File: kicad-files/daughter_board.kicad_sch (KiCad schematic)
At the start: 14 parts, among them J1 TYPE-C-31-M12_13, T1 53261-0471, U2 USBLC6-2SC6, U4 SGM2007-3.3XN5/TR

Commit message: SMall changes to the db
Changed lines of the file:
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@@
   (junction (at 133.35 147.32) (diameter 0) (color 0 0 0 0)
   )
-  (junction (at 148.59 113.03) (diameter 0) (color 0 0 0 0)
+  (junction (at 161.29 113.03) (diameter 0) (color 0 0 0 0)
   )
   (junction (at 148.59 120.65) (diameter 0) (color 0 0 0 0)
@@
   )
   (wire (pts (xy 148.59 83.82) (xy 167.64 83.82))
+    (stroke (width 0) (type default))
+  )
+  (wire (pts (xy 161.29 113.03) (xy 179.07 113.03))
     (stroke (width 0) (type default))
   )
@@
     (stroke (width 0) (type default))
   )
-  (wire (pts (xy 148.59 113.03) (xy 179.07 113.03))
-    (stroke (width 0) (type default))
-  )
   (wire (pts (xy 236.22 127) (xy 191.77 127))
     (stroke (width 0) (type default))
@@
   )
   (wire (pts (xy 243.84 71.12) (xy 248.92 71.12))
+    (stroke (width 0) (type default))
+  )
+  (wire (pts (xy 148.59 110.49) (xy 161.29 110.49))
     (stroke (width 0) (type default))
   )
@@
     (stroke (width 0) (type default))
   )
+  (wire (pts (xy 148.59 113.03) (xy 161.29 113.03))
+    (stroke (width 0) (type default))
+  )
   (wire (pts (xy 232.41 106.68) (xy 232.41 134.62))
     (stroke (width 0) (type default))
@@
     (stroke (width 0) (type default))
   )
+  (wire (pts (xy 161.29 110.49) (xy 161.29 113.03))
+    (stroke (width 0) (type default))
+  )
   (wire (pts (xy 190.5 66.04) (xy 190.5 71.12))
     (stroke (width 0) (type default))
@@
     (stroke (width 0) (type default))
   )
-  (wire (pts (xy 148.59 110.49) (xy 148.59 113.03))
-    (stroke (width 0) (type default))
-  )

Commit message: Fixed up the daughter board
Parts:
- removed U2: USBLC6-2SC6, acheron_Components:SOT-23-6, symbol Power_Protection:USBLC6-2SC6
- added D1: ESD5Z5V0, Diode_SMD:D_SOD-523, symbol Diode:SMF6V0A
- added U1: TPD4E05U06DQAR, Package_SON:USON-10_2.5x1.0mm_P0.5mm, symbol acheron_Symbols:TPD4E05U06DQAR
- D1: value B5819W-SL -> 1N5819WS; footprint Diode_SMD:D_SOD-123 -> Diode_SMD:D_SOD-323
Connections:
- net GND: now also D1.1 (A1), U1.3 (GND), U1.8 (GND)
- net 3V3: now reaches C5.1, D1.2 (A), R4.2, T1.1 (3V3), U4.5 (OUT)
- net VBUS: now reaches F1.1, J1.A4 (VBUS), J1.B4 (VBUS)
- net VBUS: now also D1.2 (A2)
- net D+: now reaches T1.2 (D+)
- net D+: now also J1.A6 (D+), J1.B6 (D+), U1.4 (D2+), U1.5 (D2-), U1.6 (NC), U1.7 (NC)
- net D-: now reaches T1.3 (D-)
- net D-: now also J1.A7 (D-), J1.B7 (D-), U1.1 (IO1), U1.10 (NC), U1.2 (IO2), U1.9 (NC)
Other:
- moved on the sheet: C3, C4, C5, D1, F1, FB1, J1, R1, R2, R3, R4, U4

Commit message: Finished daughter board
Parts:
- added MH1, MH3, MH4: Mount-M2, MountingHole:MountingHole_2.2mm_M2_Pad_TopOnly, symbol Connector_Generic:Conn_01x01
- added MH2: Mount-M2, MountingHole:MountingHole_2.2mm_M2_Pad_TopBottom, symbol Connector_Generic:Conn_01x01
- C3, C4, C5: footprint Capacitor_SMD:C_0603_1608Metric_Pad1.08x0.95mm_HandSolder -> Capacitor_SMD:C_0402_1005Metric
- D1: footprint Diode_SMD:D_SOD-323 -> Diode_SMD:D_SOD-123
- R1, R2, R3, R4: footprint Resistor_SMD:R_0603_1608Metric -> Resistor_SMD:R_0402_1005Metric
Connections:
- net GNDPWR: now also MH2.1 (Pin_1)
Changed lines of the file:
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@@
       (effects (font (size 1.27 1.27)))
     )
-    (property "Footprint" "Resistor_SMD:R_0603_1608Metric" (at 242.316 85.09 90)
+    (property "Footprint" "Resistor_SMD:R_0402_1005Metric" (at 242.316 85.09 90)
       (effects (font (size 1.27 1.27)) hide)
     )
@@
       (effects (font (size 1.27 1.27)))
     )
-    (property "Footprint" "Resistor_SMD:R_0603_1608Metric" (at 205.486 85.09 90)
+    (property "Footprint" "Resistor_SMD:R_0402_1005Metric" (at 205.486 85.09 90)
       (effects (font (size 1.27 1.27)) hide)
     )
@@
     )
   )
+  (symbol (lib_id "power:GNDPWR") (at 236.855 124.587 270) (unit 1)
+    (in_bom yes) (on_board yes) (dnp no)
+    (property "Reference" "#PWR06" (at 231.775 124.587 0)
+      (effects (font (size 1.27 1.27)) hide)
+    )
+    (property "Value" "GNDPWR" (at 234.315 124.587 0)
+      (effects (font (size 0.381 0.381)) hide)
+    )
+    (property "Footprint" "" (at 235.585 124.587 0)
+      (effects (font (size 1.27 1.27)) hide)
+    )
+    (property "Datasheet" "" (at 235.585 124.587 0)
+      (effects (font (size 1.27 1.27)) hide)
+    )
+    (pin "1")
+    (instances
+      (project "daughter_board"
+        (path "/5fbc77d5-0b17-4c7b-9496-7422d8d21889"
+          (reference "#PWR06") (unit 1)
+        )
+      )
+      (project "UDB"
+        (path "/c4c12ac1-bf97-4e49-b99b-b461a52b064e"
+          (reference "#PWR03") (unit 1)
+        )
+      )
+    )
+  )
   (symbol (lib_id "power:GND") (at 220.218 90.17 0) (unit 1)
     (in_bom yes) (on_board yes) (dnp no) (fields_autoplaced)
@@
     )
   )
+  (symbol (lib_id "Connector_Generic:Conn_01x01") (at 241.935 124.587 0) (unit 1)
+    (in_bom no) (on_board yes) (dnp no)
+    (property "Reference" "MH2" (at 243.9416 123.5202 0)
+      (effects (font (size 1.27 1.27)) (justify left))
+    )
+    (property "Value" "Mount-M2" (at 243.9416 125.8316 0)
+      (effects (font (size 1.27 1.27)) (justify left))
+    )
+    (property "Footprint" "MountingHole:MountingHole_2.2mm_M2_Pad_TopBottom" (at 241.935 124.587 0)
+      (effects (font (size 1.27 1.27)) hide)
+    )
+    (property "Datasheet" "~" (at 241.935 124.587 0)
+      (effects (font (size 1.27 1.27)) hide)
+    )
+    (pin "1")
+    (instances
+      (project "daughter_board"
+        (path "/5fbc77d5-0b17-4c7b-9496-7422d8d21889"
+          (reference "MH2") (unit 1)
+        )
+      )
+      (project "UDB"
+        (path "/c4c12ac1-bf97-4e49-b99b-b461a52b064e"
+          (reference "MH2") (unit 1)
+        )
+      )
+    )
+  )
   (symbol (lib_id "Device:D_Schottky") (at 220.218 68.58 0) (unit 1)
     (in_bom yes) (on_board yes) (dnp no) (fields_autoplaced)
@@
       (effects (font (size 1.27 1.27)))
     )
-    (property "Footprint" "Diode_SMD:D_SOD-323" (at 220.218 68.58 0)
+    (property "Footprint" "Diode_SMD:D_SOD-123" (at 220.218 68.58 0)
       (effects (font (size 1.27 1.27)) hide)
     )
@@
       (effects (font (size 1.27 1.27)) (justify left))
     )
-    (property "Footprint" "Capacitor_SMD:C_0603_1608Metric_Pad1.08x0.95mm_HandSolder" (at 251.6632 88.9 0)
+    (property "Footprint" "Capacitor_SMD:C_0402_1005Metric" (at 251.6632 88.9 0)
       (effects (font (size 1.27 1.27)) hide)
     )
@@
       (effects (font (size 1.27 1.27)))
     )
-    (property "Footprint" "Resistor_SMD:R_0603_1608Metric" (at 135.382 90.678 90)
+    (property "Footprint" "Resistor_SMD:R_0402_1005Metric" (at 135.382 90.678 90)
       (effects (font (size 1.27 1.27)) hide)
     )
@@
       (effects (font (size 1.27 1.27)) (justify left))
     )
-    (property "Footprint" "Capacitor_SMD:C_0603_1608Metric_Pad1.08x0.95mm_HandSolder" (at 198.3232 88.9 0)
+    (property "Footprint" "Capacitor_SMD:C_0402_1005Metric" (at 198.3232 88.9 0)
       (effects (font (size 1.27 1.27)) hide)
     )
@@
       (effects (font (size 1.27 1.27)) (justify left))
     )
-    (property "Footprint" "Capacitor_SMD:C_0603_1608Metric_Pad1.08x0.95mm_HandSolder" (at 235.1532 92.71 0)
+    (property "Footprint" "Capacitor_SMD:C_0402_1005Metric" (at 235.1532 92.71 0)
       (effects (font (size 1.27 1.27)) hide)
     )
@@
         (path "/5fbc77d5-0b17-4c7b-9496-7422d8d21889"
           (reference "C4") (unit 1)
+        )
+      )
+    )
+  )
+  (symbol (lib_id "Connector_Generic:Conn_01x01") (at 241.935 129.032 0) (unit 1)
+    (in_bom no) (on_board yes) (dnp no)
+    (property "Reference" "MH3" (at 243.9416 127.9652 0)
+      (effects (font (size 1.27 1.27)) (justify left))
+    )
+    (property "Value" "Mount-M2" (at 243.9416 130.2766 0)
+      (effects (font (size 1.27 1.27)) (justify left))
+    )
+    (property "Footprint" "MountingHole:MountingHole_2.2mm_M2_Pad_TopOnly" (at 241.935 129.032 0)
+      (effects (font (size 1.27 1.27)) hide)
+    )
+    (property "Datasheet" "~" (at 241.935 129.032 0)
+      (effects (font (size 1.27 1.27)) hide)
+    )
+    (pin "1")
+    (instances
+      (project "daughter_board"
+        (path "/5fbc77d5-0b17-4c7b-9496-7422d8d21889"
+          (reference "MH3") (unit 1)
+        )
+      )
+      (project "UDB"
+        (path "/c4c12ac1-bf97-4e49-b99b-b461a52b064e"
+          (reference "MH3") (unit 1)
         )
       )
@@
       (effects (font (size 1.27 1.27)))
     )
-    (property "Footprint" "Resistor_SMD:R_0603_1608Metric" (at 135.382 95.758 90)
+    (property "Footprint" "Resistor_SMD:R_0402_1005Metric" (at 135.382 95.758 90)
       (effects (font (size 1.27 1.27)) hide)
     )
@@
     )
   )
+  (symbol (lib_id "Connector_Generic:Conn_01x01") (at 241.935 133.477 0) (unit 1)
+    (in_bom no) (on_board yes) (dnp no)
+    (property "Reference" "MH4" (at 243.9416 132.4102 0)
+      (effects (font (size 1.27 1.27)) (justify left))
+    )
+    (property "Value" "Mount-M2" (at 243.9416 134.7216 0)
+      (effects (font (size 1.27 1.27)) (justify left))
+    )
+    (property "Footprint" "MountingHole:MountingHole_2.2mm_M2_Pad_TopOnly" (at 241.935 133.477 0)
+      (effects (font (size 1.27 1.27)) hide)
+    )
+    (property "Datasheet" "~" (at 241.935 133.477 0)
+      (effects (font (size 1.27 1.27)) hide)
+    )
+    (pin "1")
+    (instances
+      (project "daughter_board"
+        (path "/5fbc77d5-0b17-4c7b-9496-7422d8d21889"
+          (reference "MH4") (unit 1)
+        )
+      )
+      (project "UDB"
+        (path "/c4c12ac1-bf97-4e49-b99b-b461a52b064e"
+          (reference "MH4") (unit 1)
+        )
+      )
+    )
+  )
   (symbol (lib_id "power:GNDPWR") (at 142.494 143.256 180) (unit 1)
     (in_bom yes) (on_board yes) (dnp no) (fields_autoplaced)
@@
         )
       )
+    )
+  )
+  (symbol (lib_id "Connector_Generic:Conn_01x01") (at 241.935 120.142 0) (unit 1)
+    (in_bom no) (on_board yes) (dnp no)
+    (property "Reference" "MH1" (at 243.9416 119.0752 0)
+      (effects (font (size 1.27 1.27)) (justify left))
+    )
+    (property "Value" "Mount-M2" (at 243.9416 121.3866 0)
+      (effects (font (size 1.27 1.27)) (justify left))
+    )
+    (property "Footprint" "MountingHole:MountingHole_2.2mm_M2_Pad_TopOnly" (at 241.935 120.142 0)
+      (effects (font (size 1.27 1.27)) hide)
+    )
+    (property "Datasheet" "~" (at 241.935 120.142 0)
+      (effects (font (size 1.27 1.27)) hide)
+    )
+    (pin "1")
+    (instances
+      (project "daughter_board"
+        (path "/5fbc77d5-0b17-4c7b-9496-7422d8d21889"
+          (reference "MH1") (unit 1)
+        )
+      )
+      (project "UDB"
+        (path "/c4c12ac1-bf97-4e49-b99b-b461a52b064e"
+          (reference "MH1") (unit 1)
+        )
+      )

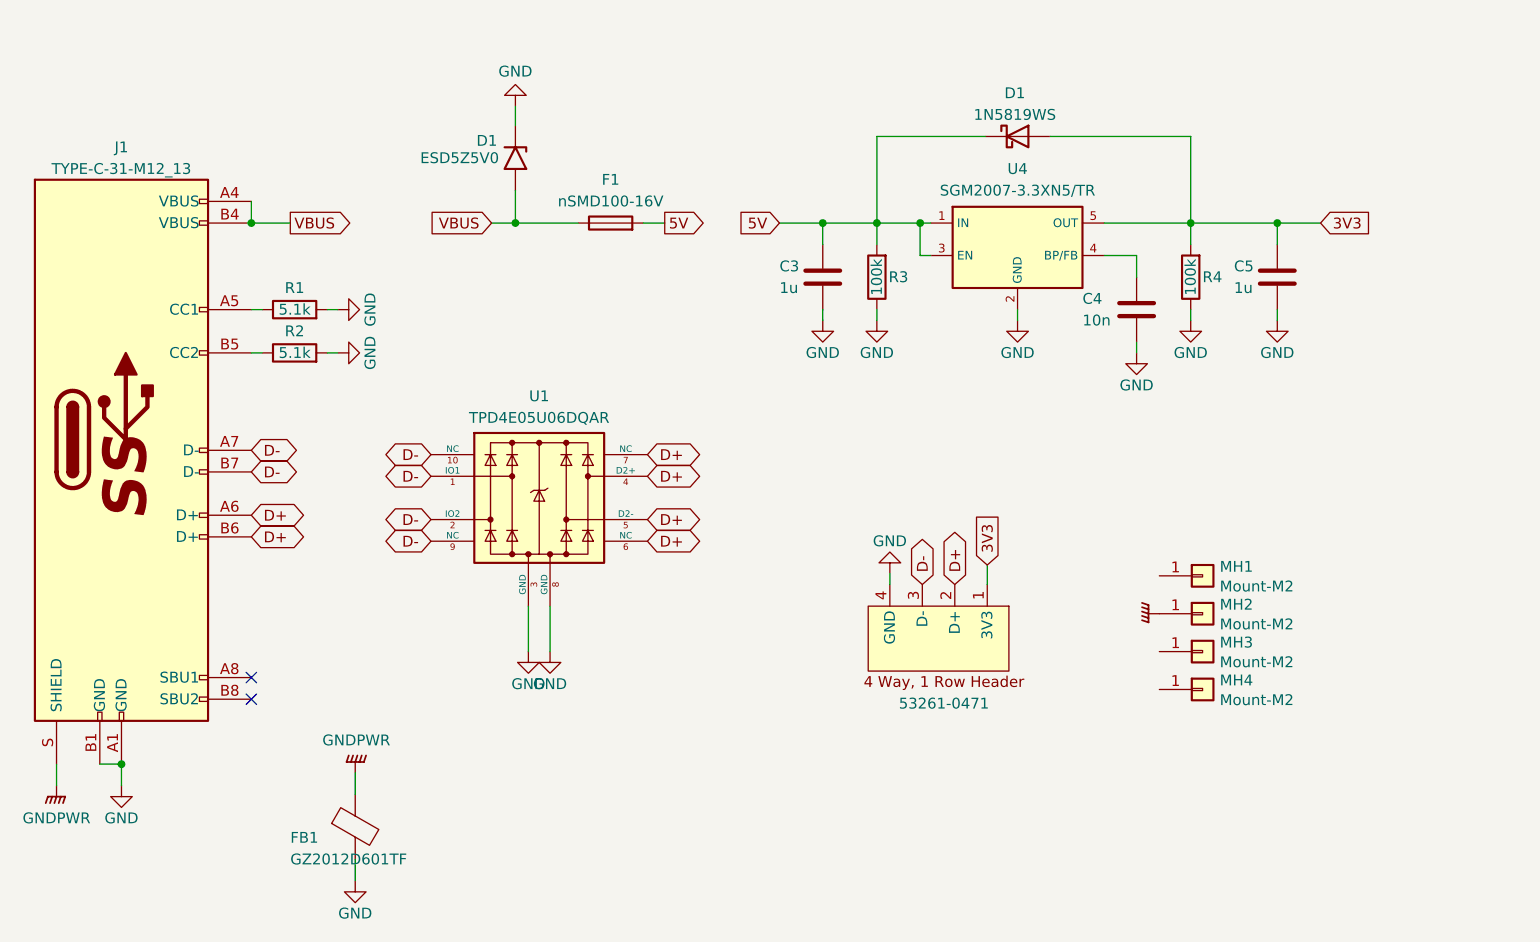
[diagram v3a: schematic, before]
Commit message: Fixing up the schematic's of daughter and mother boards
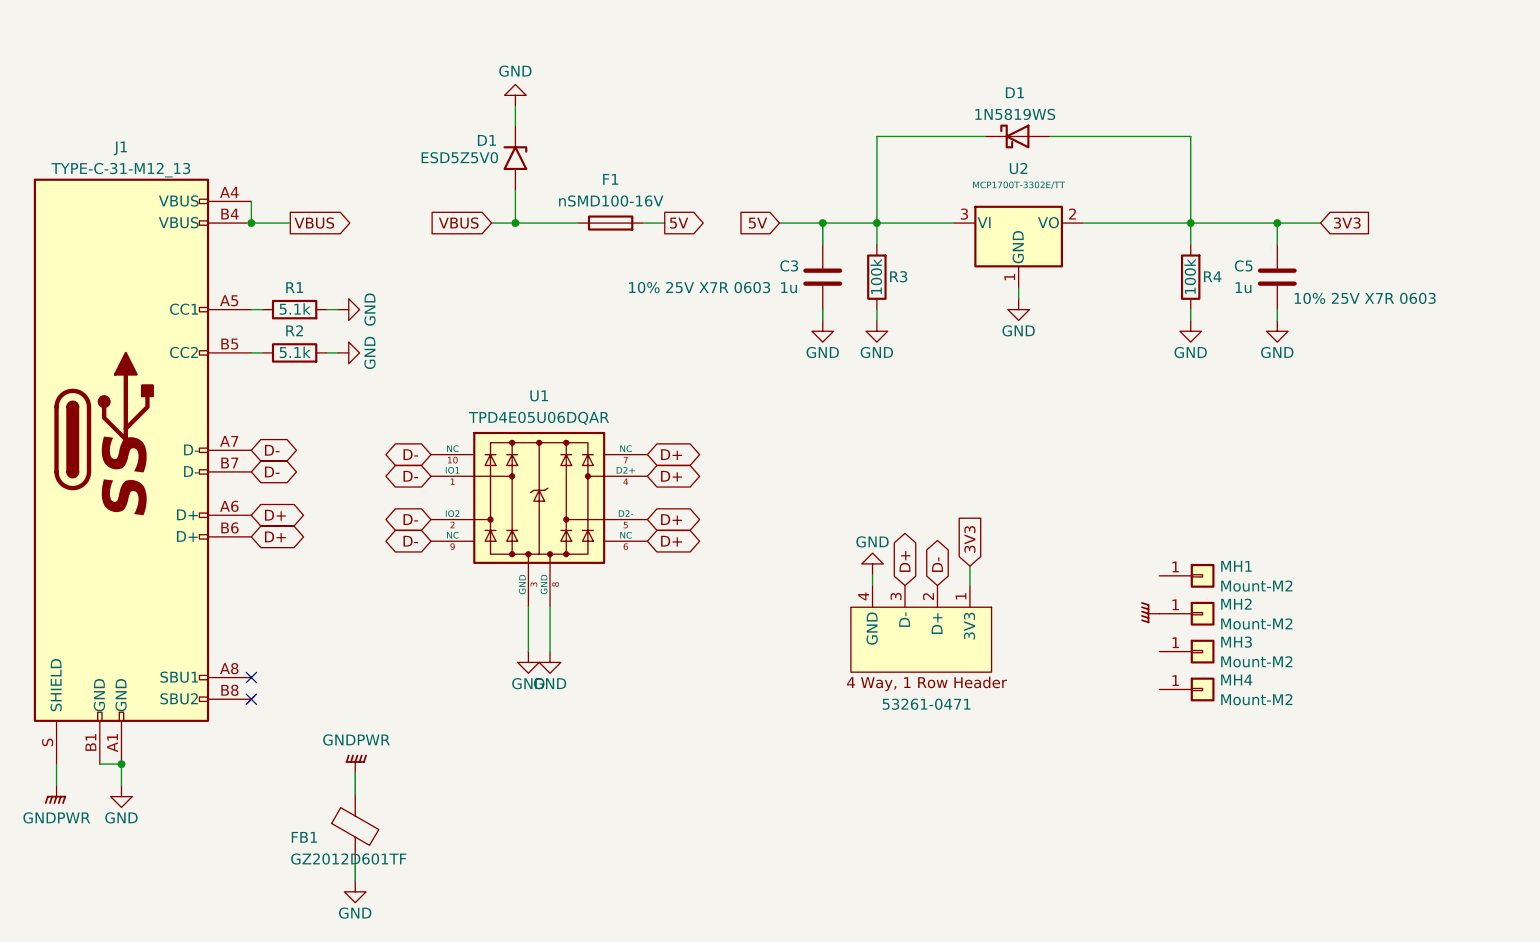
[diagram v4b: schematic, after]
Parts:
- removed C4: 10n, Capacitor_SMD:C_0402_1005Metric, symbol Device:C
- removed U4: SGM2007-3.3XN5/TR, acheron_Components:SOT-23-5, symbol acheron_Symbols:SGM2036
- added U2: MCP1700T-3302E/TT, Package_TO_SOT_SMD:SOT-23, symbol Regulator_Linear:MCP1700-3302E_SOT23
- C3, C5: footprint Capacitor_SMD:C_0402_1005Metric -> Capacitor_SMD:C_0603_1608Metric; Package (none) -> 0603; Specification (none) -> 10% 25V X7R 0603
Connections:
- net 3V3: now also U2.2 (VO)
- net 5V: now also U2.3 (VI)
- net D+: now also T1.3 (D-); no longer T1.2 (D+)
- net D-: now also T1.2 (D+); no longer T1.3 (D-)
- net GND: now also U2.1 (GND)

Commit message: Added legshark logo to the daugherboard
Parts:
- added H1: LegSharkLogo, Legshark:Legshark_Small_Mask, symbol Mechanical:MountingHole
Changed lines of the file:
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@@
+    )
+  )
+  (symbol (lib_id "Mechanical:MountingHole") (at 203.835 146.685 0) (unit 1)
+    (in_bom yes) (on_board yes) (dnp no) (fields_autoplaced)
+    (property "Reference" "H1" (at 207.01 146.05 0)
+      (effects (font (size 1.27 1.27)) (justify left))
+    )
+    (property "Value" "LegSharkLogo" (at 207.01 148.59 0)
+      (effects (font (size 1.27 1.27)) (justify left))
+    )
+    (property "Footprint" "Legshark:Legshark_Small_Mask" (at 203.835 146.685 0)
+      (effects (font (size 1.27 1.27)) hide)
+    )
+    (property "Datasheet" "~" (at 203.835 146.685 0)
+      (effects (font (size 1.27 1.27)) hide)
+    )
+    (instances
+      (project "daughter_board"
+        (path "/5fbc77d5-0b17-4c7b-9496-7422d8d21889"
+          (reference "H1") (unit 1)
+        )
+      )
     )
   )

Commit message: Added parts
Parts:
- C3, C5: value 1u -> 1uF; LCSC Part (none) -> C90540; Manufacturer (none) -> Guangdong Fenghua Advanced Tech; Manufacturer Part Number (none) -> 0603B105K500NT; Specification 10% 25V X7R 0603 -> 50V 1uF X7R ±10% 0603
- F1: value nSMD100-16V -> SMD0805-050-16V; LCSC Part Number (none) -> C2833485; Manufacturer Part Number (none) -> SMD0805-050-16V; Package (none) -> F0805
- FB1: Manufacturer Part Number (none) -> GZ2012D601TF; Package (none) -> F0805
- J1: value TYPE-C-31-M12_13 -> TYPE-C-31-M-12; LCSC Part Number (none) -> C165948; Manufacturer (none) -> Koren Hroparts; Manufacturer Part Number (none) -> TYPE-C-31-M-12
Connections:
- net GND: now also D1.2 (A2); no longer D1.1 (A1)
- net VBUS: now also D1.1 (A1); no longer D1.2 (A2)
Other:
- moved on the sheet: C3, C5, D1, R3, R4, U2

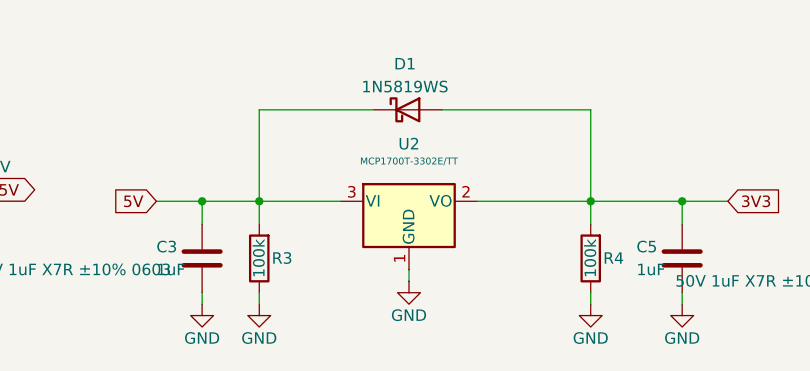
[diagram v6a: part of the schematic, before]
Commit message: Finished adding parts to the daughter board
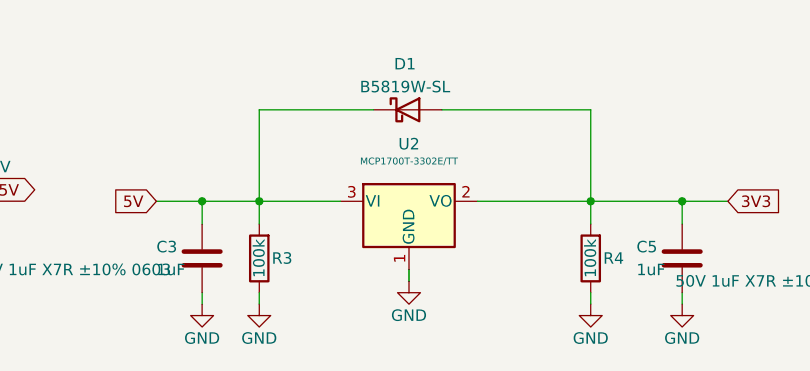
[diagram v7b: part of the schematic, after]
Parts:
- D1: value 1N5819WS -> B5819W-SL; Manufacturer (none) -> Changjiang Electronics Tech; Package (none) -> SOD-123; Specification (none) -> 1A SOD-123 Schottky Barrier Diodes; Vendor Part Number (none) -> LCSC C8598
- R3, R4: LCSC Part (none) -> C606167; Manufacturer (none) -> YAGEO; Package (none) -> 0402; Specification (none) -> 125mW Thick Film Resistors ±1% 100kΩ 0402
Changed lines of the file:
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@@
+      (effects (font (size 1.27 1.27)) hide)
+    )
+    (property "LCSC Part" "C606167" (at 245.11 86.36 0)
+      (effects (font (size 1.27 1.27)) hide)
+    )
+    (property "Package" "0402" (at 245.11 86.36 0)
+      (effects (font (size 1.27 1.27)) hide)
+    )
+    (property "Specification" "125mW Thick Film Resistors ±1% 100kΩ 0402" (at 245.11 86.36 0)
+      (effects (font (size 1.27 1.27)) hide)
+    )
+    (property "Manufacturer" "YAGEO" (at 245.11 86.36 0)
       (effects (font (size 1.27 1.27)) hide)
     )
@@
       (effects (font (size 1.27 1.27)) hide)
     )
+    (property "LCSC Part" "C606167" (at 208.28 86.36 0)
+      (effects (font (size 1.27 1.27)) hide)
+    )
+    (property "Package" "0402" (at 208.28 86.36 0)
+      (effects (font (size 1.27 1.27)) hide)
+    )
+    (property "Specification" "125mW Thick Film Resistors ±1% 100kΩ 0402" (at 208.28 86.36 0)
+      (effects (font (size 1.27 1.27)) hide)
+    )
+    (property "Manufacturer" "YAGEO" (at 208.28 86.36 0)
+      (effects (font (size 1.27 1.27)) hide)
+    )
     (pin "1")
     (pin "2")
@@
       (effects (font (size 1.27 1.27)))
     )
-    (property "Value" "1N5819WS" (at 224.4725 67.31 0)
+    (property "Value" "B5819W-SL" (at 224.4725 67.31 0)
       (effects (font (size 1.27 1.27)))
     )
@@
       (effects (font (size 1.27 1.27)) hide)
     )
-    (property "Datasheet" "https://datasheet.lcsc.com/lcsc/2204281430_Guangdong-Hottech-1N5819WS_C191023.pdf" (at 224.79 69.85 0)
-      (effects (font (size 1.27 1.27)) hide)
-    )
+    (property "Datasheet" "~" (at 224.79 69.85 0)
+      (effects (font (size 1.27 1.27)) hide)
+    )
+    (property "Package" "SOD-123" (at 224.79 69.85 0)
+      (effects (font (size 1.27 1.27)) hide)
+    )
+    (property "Vendor Part Number" "LCSC C8598" (at 224.79 69.85 0)
+      (effects (font (size 1.27 1.27)) hide)
+    )
+    (property "Manufacturer" "Changjiang Electronics Tech" (at 224.79 69.85 0)
+      (effects (font (size 1.27 1.27)) hide)
+    )
+    (property "Specification" "1A SOD-123 Schottky Barrier Diodes" (at 224.79 69.85 0)
+      (effects (font (size 1.27 1.27)) hide)
+    )
